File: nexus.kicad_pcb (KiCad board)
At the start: 2 copper layers, 100 x 125 mm, 114 parts, among them J1 PIN6-9_Breakout, J10 Screw_Terminal_01x02, J11 24V_Lockout_Key_Switch, J12 XT60-M, J13 PT_1, J14 PT_4, J15 PT_2, J16 PT_5, J17 PT_3, J18 PT_6, J19 4-Pin Load Cell, J2 PIN10-13_Breakout, J20 5-Pin Load Cell, J21 Ignitor Screw Terminal, J3 Valve_1_PWR, J4 Valve_4_PWR, J5 Valve_2_PWR, J6 Valve_5_PWR, J7 Valve_3_PWR, J8 Valve_6_PWR, J9 Screw_Terminal_01x04, K1 G5LE-1, K2 G5LE-1, Q1 BSS138, Q2 BSS138, Q3 BSS138, Q4 BSS138, Q5 BSS138, Q6 BSS138, Q7 BSS138, Q8 BSS138, U1 ESP32-S3, U2 ADS112C04, U3 ADS112C04, U4 ADS112C04, U5 ADS112C04, U6 XC6206P332MR, U7 TPS5430DDA, U8 TPS5430DDA

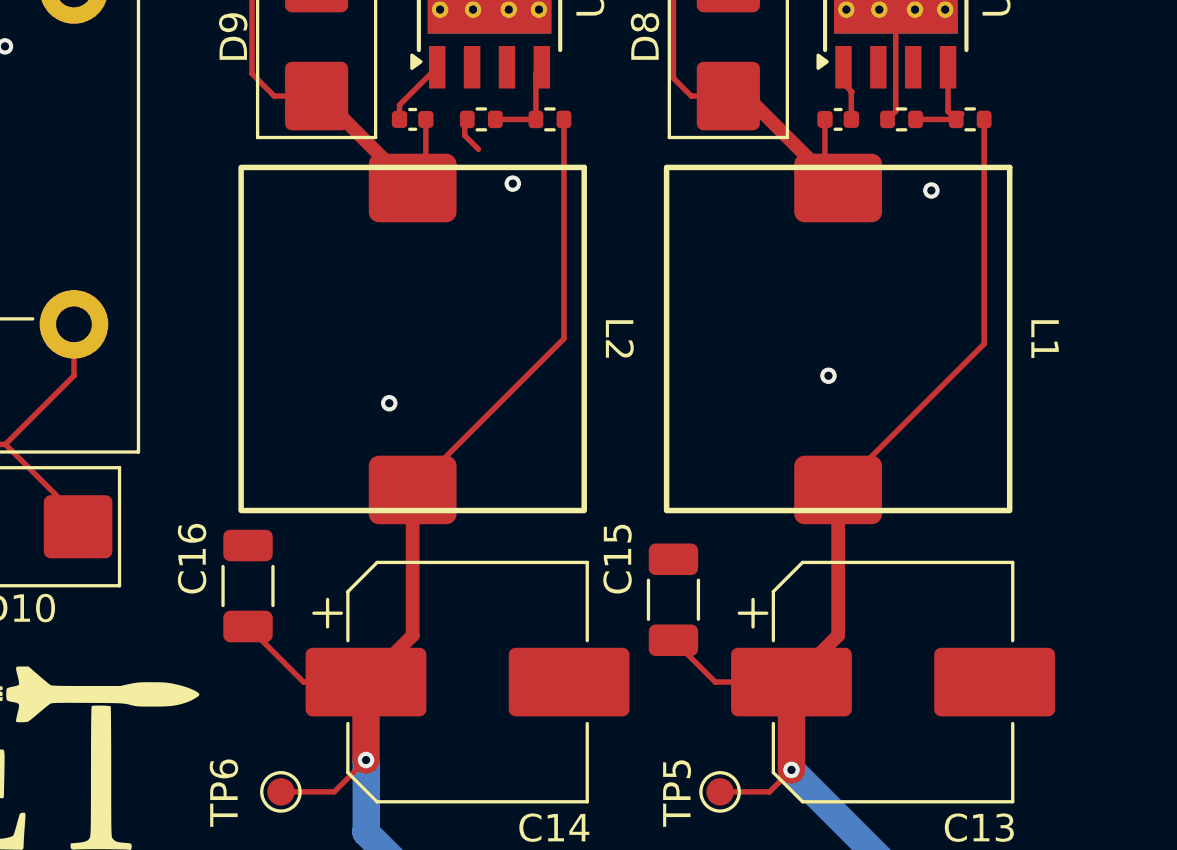
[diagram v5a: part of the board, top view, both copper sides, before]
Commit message: Fix inductor layout
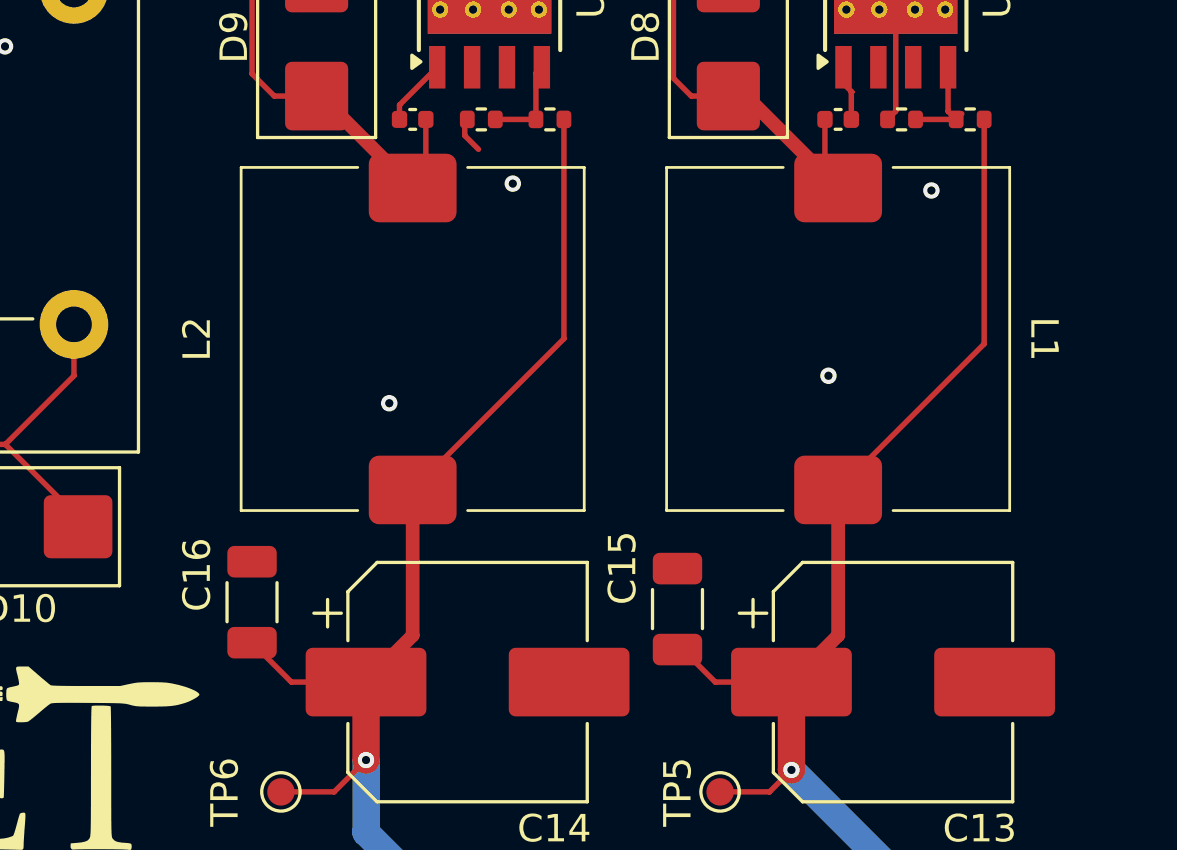
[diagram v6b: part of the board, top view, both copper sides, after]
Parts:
- moved C16 0.61 mm to (172.2, 58.0)
- moved C15 0.37 mm to (187.8, 58.2)
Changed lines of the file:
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@@
 	(footprint "Capacitor_SMD:C_1206_3216Metric"
 		(layer "F.Cu")
-		(at 172.102501 57.41 90)
+		(at 172.25 58 90)
 		(descr "Capacitor SMD 1206 (3216 Metric), square (rectangular) end terminal, IPC_7351 nominal, (Body size source: IPC-SM-782 page 76, https://www.pcb-3d.com/wordpress/wp-content/uploads/ipc-sm-782a_amendment_1_and_2.pdf), generated with kicad-footprint-generator")
 		(tags "capacitor")
@@
 	(footprint "Capacitor_SMD:C_1206_3216Metric"
 		(layer "F.Cu")
-		(at 187.602501 57.91 90)
+		(at 187.75 58.25 90)
 		(descr "Capacitor SMD 1206 (3216 Metric), square (rectangular) end terminal, IPC_7351 nominal, (Body size source: IPC-SM-782 page 76, https://www.pcb-3d.com/wordpress/wp-content/uploads/ipc-sm-782a_amendment_1_and_2.pdf), generated with kicad-footprint-generator")
 		(tags "capacitor")
@@
 		(sheetfile "PowerRegulation.kicad_sch")
 		(attr smd)
+		(fp_line
+			(start -6.25 6.25)
+			(end -6.25 2)
+			(stroke
+				(width 0.1)
+				(type default)
+			)
+			(layer "F.SilkS")
+		)
+		(fp_line
+			(start 6.25 6.25)
+			(end -6.25 6.25)
+			(stroke
+				(width 0.1)
+				(type default)
+			)
+			(layer "F.SilkS")
+		)
+		(fp_line
+			(start 6.25 6.25)
+			(end 6.25 2)
+			(stroke
+				(width 0.1)
+				(type default)
+			)
+			(layer "F.SilkS")
+		)
+		(fp_line
+			(start -6.25 -6.25)
+			(end -6.25 -2)
+			(stroke
+				(width 0.1)
+				(type default)
+			)
+			(layer "F.SilkS")
+		)
+		(fp_line
+			(start -6.25 -6.25)
+			(end 6.25 -6.25)
+			(stroke
+				(width 0.1)
+				(type default)
+			)
+			(layer "F.SilkS")
+		)
+		(fp_line
+			(start 6.25 -6.25)
+			(end 6.25 -2)
+			(stroke
+				(width 0.1)
+				(type default)
+			)
+			(layer "F.SilkS")
+		)
+		(fp_rect
+			(start -7 -7)
+			(end 7 7)
+			(stroke
+				(width 0.05)
+				(type default)
+			)
+			(fill no)
+			(layer "F.CrtYd")
+		)
 		(fp_rect
 			(start -6.25 -6.25)
@@
 			)
 			(fill no)
-			(layer "F.SilkS")
+			(layer "F.Fab")
 		)
 		(fp_text user "${REFERENCE}"
@@
 		(at 178.102501 48.41 -90)
 		(property "Reference" "L2"
-			(at 0 -7.5 270)
+			(at 0 7.852501 90)
 			(unlocked yes)
 			(layer "F.SilkS")
@@
 		(sheetfile "PowerRegulation.kicad_sch")
 		(attr smd)
+		(fp_line
+			(start -6.25 6.25)
+			(end -6.25 2)
+			(stroke
+				(width 0.1)
+				(type default)
+			)
+			(layer "F.SilkS")
+		)
+		(fp_line
+			(start 6.25 6.25)
+			(end -6.25 6.25)
+			(stroke
+				(width 0.1)
+				(type default)
+			)
+			(layer "F.SilkS")
+		)
+		(fp_line
+			(start 6.25 6.25)
+			(end 6.25 2)
+			(stroke
+				(width 0.1)
+				(type default)
+			)
+			(layer "F.SilkS")
+		)
+		(fp_line
+			(start -6.25 -6.25)
+			(end -6.25 -2)
+			(stroke
+				(width 0.1)
+				(type default)
+			)
+			(layer "F.SilkS")
+		)
+		(fp_line
+			(start -6.25 -6.25)
+			(end 6.25 -6.25)
+			(stroke
+				(width 0.1)
+				(type default)
+			)
+			(layer "F.SilkS")
+		)
+		(fp_line
+			(start 6.25 -6.25)
+			(end 6.25 -2)
+			(stroke
+				(width 0.1)
+				(type default)
+			)
+			(layer "F.SilkS")
+		)
+		(fp_rect
+			(start -7 -7)
+			(end 7 7)
+			(stroke
+				(width 0.05)
+				(type default)
+			)
+			(fill no)
+			(layer "F.CrtYd")
+		)
 		(fp_rect
 			(start -6.25 -6.25)
@@
 			)
 			(fill no)
-			(layer "F.SilkS")
+			(layer "F.Fab")
 		)
 		(fp_text user "${REFERENCE}"
@@
 	)
 	(segment
+		(start 176.402501 60.91)
+		(end 173.685 60.91)
+		(width 0.2)
+		(layer "F.Cu")
+		(net 3)
+	)
+	(segment
 		(start 175.242501 64.91)
 		(end 176.402501 63.75)
@@
 	)
 	(segment
-		(start 183.612501 48.4)
-		(end 183.612501 40.41)
+		(start 173.685 60.91)
+		(end 172.25 59.475)
 		(width 0.2)
 		(layer "F.Cu")
@@
 	)
 	(segment
-		(start 174.127501 60.91)
-		(end 172.102501 58.885)
+		(start 183.612501 48.4)
+		(end 183.612501 40.41)
 		(width 0.2)
 		(layer "F.Cu")
@@
 		(layer "F.Cu")
 		(net 3)
-	)
-	(segment
-		(start 176.402501 60.91)
-		(end 174.127501 60.91)
-		(width 0.2)
-		(layer "F.Cu")
-		(net 3)

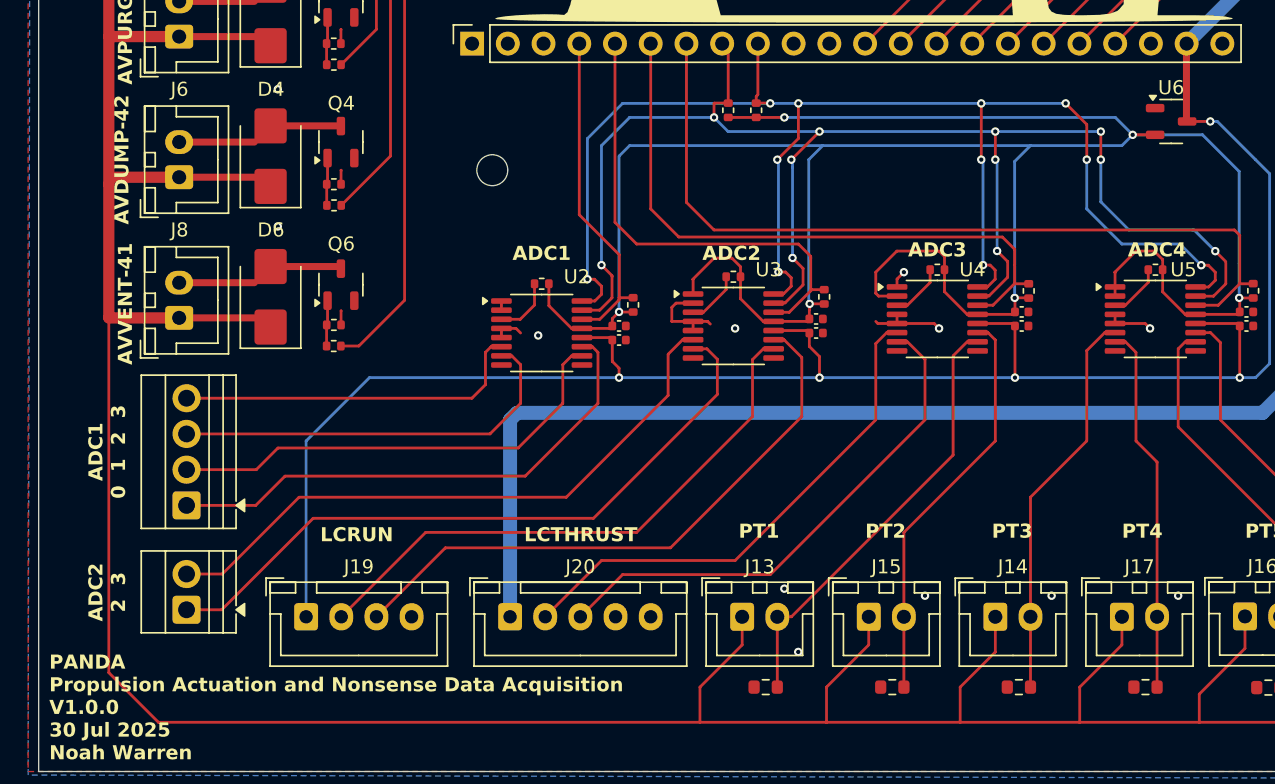
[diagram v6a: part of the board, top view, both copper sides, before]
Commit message: Fix silk screening
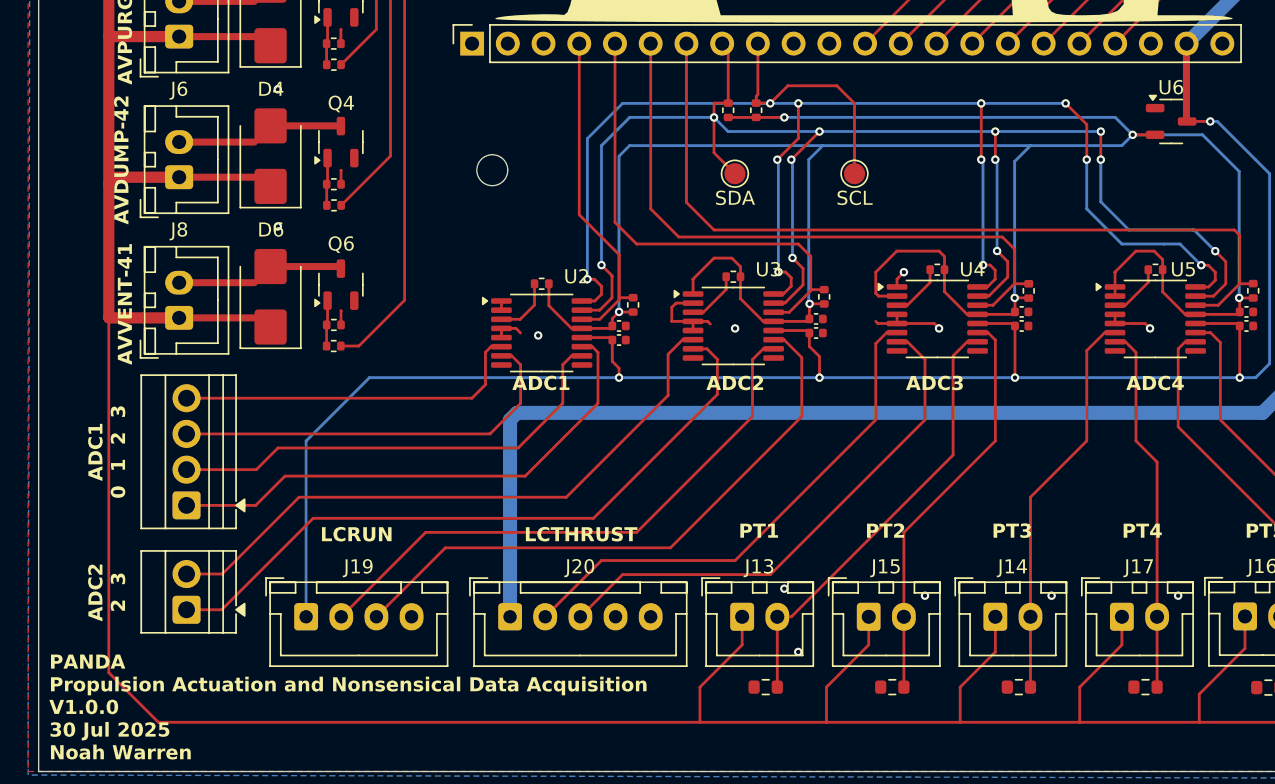
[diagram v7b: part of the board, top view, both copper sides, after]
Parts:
- added SCL: SCL, TestPoint:TestPoint_Pad_D1.5mm, F.Cu at (168.2, 107.2)
- added SDA: SDA, TestPoint:TestPoint_Pad_D1.5mm, F.Cu at (159.8, 107.2)
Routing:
- net I2C_SCL: track 105.5 -> 117.5 mm
- net I2C_SDA: track 104.6 -> 109.2 mm
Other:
- board text added: "PANDA Propulsion Actuation and Nonsensical Data Acquisition V1.0.0 30 Jul 2025 Noah Warren"
- board text removed: "PANDA Propulsion Actuation and Nonsense Data Acquisition V1.0.0 30 Jul 2025 Noah Warren"
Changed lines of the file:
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@@
 		)
 	)
+	(footprint "TestPoint:TestPoint_Pad_D1.5mm"
+		(layer "F.Cu")
+		(at 168.25 107.25)
+		(descr "SMD pad as test Point, diameter 1.5mm")
+		(tags "test point SMD pad")
+		(property "Reference" "SCL"
+			(at 0 1.75 0)
+			(layer "F.SilkS")
+			(effects
+				(font
+					(size 1 1)
+					(thickness 0.15)
+				)
+			)
+		)
+		(property "Value" "SCL"
+			(at 0 1.75 0)
+			(layer "F.Fab")
+			(effects
+				(font
+					(size 1 1)
+					(thickness 0.15)
+				)
+			)
+		)
+		(property "Datasheet" ""
+			(at 0 0 0)
+			(unlocked yes)
+			(layer "F.Fab")
+			(hide yes)
+			(effects
+				(font
+					(size 1.27 1.27)
+					(thickness 0.15)
+				)
+			)
+		)
+		(property "Description" "test point"
+			(at 0 0 0)
+			(unlocked yes)
+			(layer "F.Fab")
+			(hide yes)
+			(effects
+				(font
+					(size 1.27 1.27)
+					(thickness 0.15)
+				)
+			)
+		)
+		(property ki_fp_filters "Pin* Test*")
+		(sheetname "/ESP32 Breakout/")
+		(sheetfile "ESP32Breakout.kicad_sch")
+		(attr exclude_from_pos_files)
+		(fp_circle
+			(center 0 0)
+			(end 0 0.95)
+			(stroke
+				(width 0.12)
+				(type solid)
+			)
+			(fill no)
+			(layer "F.SilkS")
+		)
+		(fp_circle
+			(center 0 0)
+			(end 1.25 0)
+			(stroke
+				(width 0.05)
+				(type solid)
+			)
+			(fill no)
+			(layer "F.CrtYd")
+		)
+		(fp_text user "${REFERENCE}"
+			(at 0 -1.65 0)
+			(layer "F.Fab")
+			(effects
+				(font
+					(size 1 1)
+					(thickness 0.15)
+				)
+			)
+		)
+		(pad "1" smd circle
+			(at 0 0)
+			(size 1.5 1.5)
+			(layers "F.Cu" "F.Mask")
+			(net 43 "I2C_SCL")
+			(pinfunction "1")
+			(pintype "passive")
+		)
+		(embedded_fonts no)
+	)
 	(footprint "Connector_JST:JST_XH_B2B-XH-A_1x02_P2.50mm_Vertical"
 		(layer "F.Cu")
@@
 		)
 		(property "Value" "10k"
-			(at 0 1.17 0)
+			(at 0.852501 -1.34 0)
 			(layer "F.Fab")
 			(effects
@@
 		)
 	)
+	(footprint "TestPoint:TestPoint_Pad_D1.5mm"
+		(layer "F.Cu")
+		(at 159.75 107.25)
+		(descr "SMD pad as test Point, diameter 1.5mm")
+		(tags "test point SMD pad")
+		(property "Reference" "SDA"
+			(at 0 1.75 0)
+			(layer "F.SilkS")
+			(effects
+				(font
+					(size 1 1)
+					(thickness 0.15)
+				)
+			)
+		)
+		(property "Value" "SDA"
+			(at 0 1.75 0)
+			(layer "F.Fab")
+			(effects
+				(font
+					(size 1 1)
+					(thickness 0.15)
+				)
+			)
+		)
+		(property "Datasheet" ""
+			(at 0 0 0)
+			(unlocked yes)
+			(layer "F.Fab")
+			(hide yes)
+			(effects
+				(font
+					(size 1.27 1.27)
+					(thickness 0.15)
+				)
+			)
+		)
+		(property "Description" "test point"
+			(at 0 0 0)
+			(unlocked yes)
+			(layer "F.Fab")
+			(hide yes)
+			(effects
+				(font
+					(size 1.27 1.27)
+					(thickness 0.15)
+				)
+			)
+		)
+		(property ki_fp_filters "Pin* Test*")
+		(sheetname "/ESP32 Breakout/")
+		(sheetfile "ESP32Breakout.kicad_sch")
+		(attr exclude_from_pos_files)
+		(fp_circle
+			(center 0 0)
+			(end 0 0.95)
+			(stroke
+				(width 0.12)
+				(type solid)
+			)
+			(fill no)
+			(layer "F.SilkS")
+		)
+		(fp_circle
+			(center 0 0)
+			(end 1.25 0)
+			(stroke
+				(width 0.05)
+				(type solid)
+			)
+			(fill no)
+			(layer "F.CrtYd")
+		)
+		(fp_text user "${REFERENCE}"
+			(at 0 -1.65 0)
+			(layer "F.Fab")
+			(effects
+				(font
+					(size 1 1)
+					(thickness 0.15)
+				)
+			)
+		)
+		(pad "1" smd circle
+			(at 0 0)
+			(size 1.5 1.5)
+			(layers "F.Cu" "F.Mask")
+			(net 42 "I2C_SDA")
+			(pinfunction "1")
+			(pintype "passive")
+		)
+		(embedded_fonts no)
+	)
 	(footprint "Capacitor_SMD:C_0402_1005Metric"
 		(layer "F.Cu")
@@
 	)
 	(gr_text "ADC3"
-		(at 174.1375 113.25 0)
+		(at 173.983859 122.75 0)
 		(layer "F.SilkS")
 		(effects
@@
 	)
 	(gr_text "ADC4"
-		(at 189.762501 113.25 0)
+		(at 189.6475 122.75 0)
 		(layer "F.SilkS")
 		(effects
@@
 	)
 	(gr_text "ADC2"
-		(at 159.512501 113.5 0)
+		(at 159.791141 122.75 0)
 		(layer "F.SilkS")
 		(effects
@@
 	)
 	(gr_text "ADC1"
-		(at 146.012501 113.5 0)
+		(at 146 122.75 0)
 		(layer "F.SilkS")
 		(effects
@@
 		)
 	)
-	(gr_text "PANDA\nPropulsion Actuation and Nonsense Data Acquisition\nV1.0.0\n30 Jul 2025\nNoah Warren"
+	(gr_text "PANDA\nPropulsion Actuation and Nonsensical Data Acquisition\nV1.0.0\n30 Jul 2025\nNoah Warren"
 		(at 111 149 0)
 		(layer "F.SilkS")
@@
 	)
 	(segment
+		(start 158.262501 105.762501)
+		(end 158.262501 103.25)
+		(width 0.2)
+		(layer "F.Cu")
+		(net 42)
+	)
+	(segment
 		(start 159.272501 102.23)
 		(end 158.282501 102.23)
@@
 	)
 	(segment
+		(start 159.75 107.25)
+		(end 158.262501 105.762501)
+		(width 0.2)
+		(layer "F.Cu")
+		(net 42)
+	)
+	(segment
 		(start 177.806415 115.943585)
 		(end 179.138548 114.611452)
@@
 	)
 	(segment
+		(start 167 101)
+		(end 168.25 102.25)
+		(width 0.2)
+		(layer "F.Cu")
+		(net 43)
+	)
+	(segment
 		(start 164.262501 104.75)
 		(end 164.262501 102.25)
@@
 	)
 	(segment
+		(start 163.512501 101)
+		(end 167 101)
+		(width 0.2)
+		(layer "F.Cu")
+		(net 43)
+	)
+	(segment
 		(start 193.90035 114.829568)
 		(end 193.90035 114.25457)
@@
 	)
 	(segment
+		(start 162.262501 102.25)
+		(end 163.512501 101)
+		(width 0.2)
+		(layer "F.Cu")
+		(net 43)
+	)
+	(segment
 		(start 193.425348 115.30457)
 		(end 192.512848 115.30457)
@@
 		(width 0.2)
 		(layer "F.Cu")
+		(net 43)
+	)
+	(segment
+		(start 168.25 107.25)
+		(end 168.25 102.25)
+		(width 0.2)
+		(layer "F.Cu")
